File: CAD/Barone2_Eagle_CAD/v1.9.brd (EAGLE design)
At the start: 101.6 x 101.6 mm, 71 parts, among them J2 XT60-M, M1 PIC32MX340F512H-80I/MR, U1 FT232RQ, X1 CB3LV-3C-8M0000, Y1 ABRACON_ASEK-32_768KHZ-LRTABR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

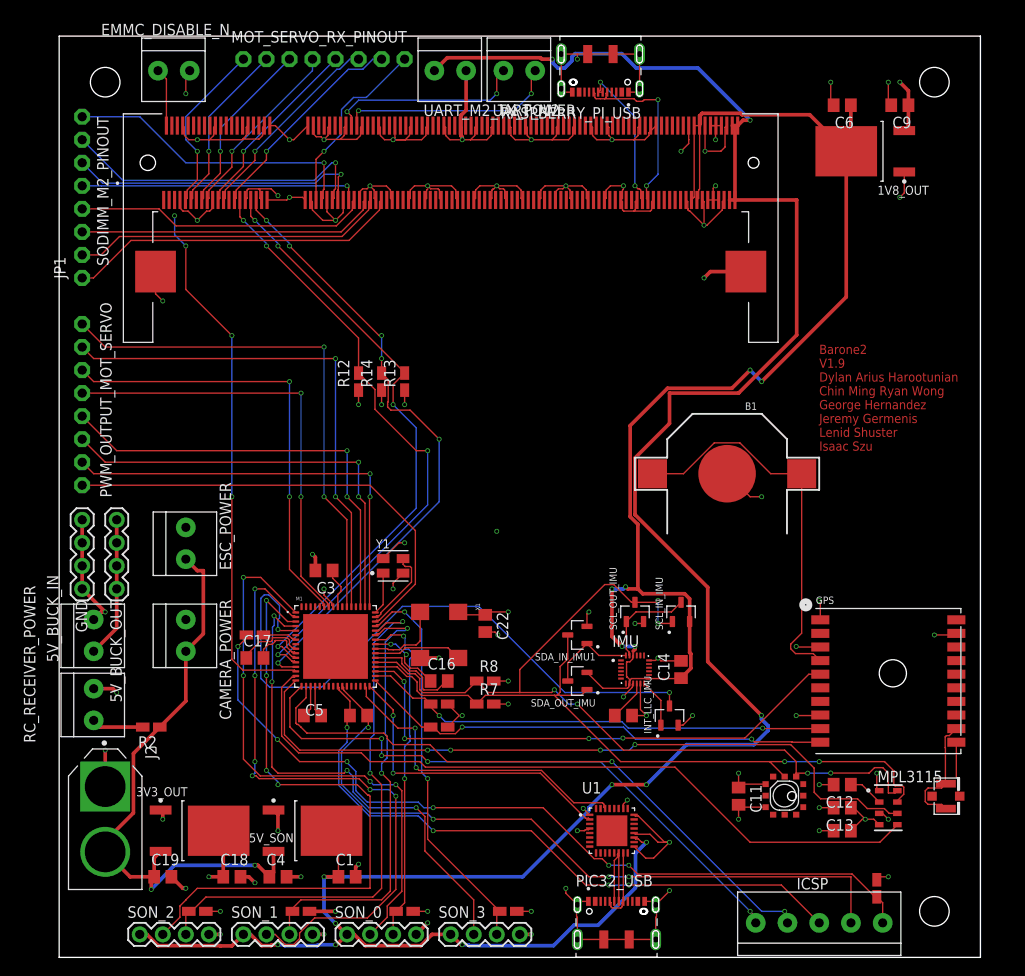
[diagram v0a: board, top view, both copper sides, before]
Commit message: v1.9 finalized and sent to board house OSH Park
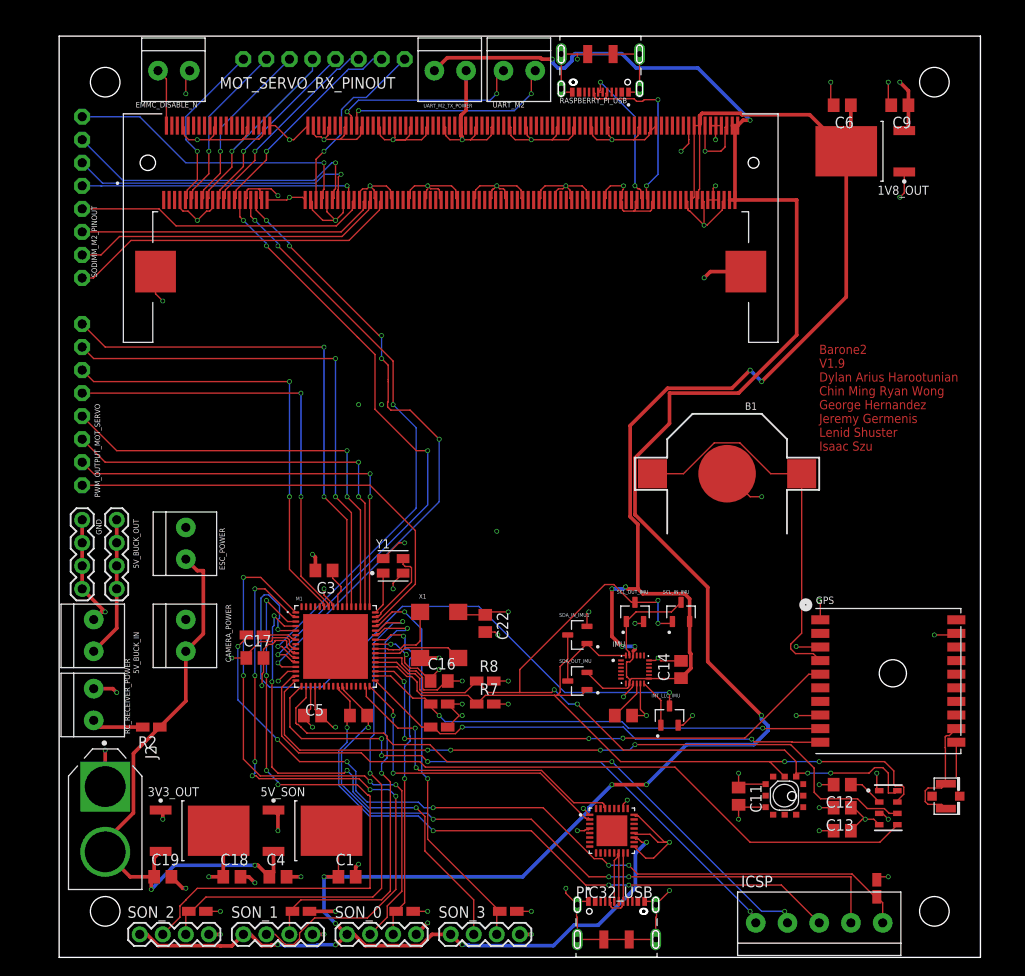
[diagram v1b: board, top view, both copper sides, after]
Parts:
- removed R12, R13, R14: 47k, adafruit:R0805W
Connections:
- removed net AVDD3_M1: C16.2, M1.38
- removed net AVDD_M1: C5.2, M1.19
- removed net AVSS_M1: C5.1, M1.20
- removed net CS_M1: M1.14
- removed net VDD1_M1: C17.2, M1.10
- removed net VDD2_M1: C15.2, ICSP.2, M1.26
- removed net VSS1_M1: C17.1, M1.9
- removed net VSS2_M1: C15.1, ICSP.3, M1.25
- removed net VSS3_M1: C16.1, M1.41
- net GND: now also C15.1, C16.1, C17.1, C5.1, ICSP.3, M1.14, M1.20, M1.25, M1.41, M1.9
- net MISO_M2: no longer R12.2
- net MOSI_M2: no longer R13.2
- net SCK_M2: no longer R14.2
- net VIN: now also C15.2, C16.2, C17.2, C5.2, ICSP.2, M1.10, M1.19, M1.26, M1.38; no longer R12.1, R13.1, R14.1
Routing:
- net GND: track 919.8 -> 1046.8 mm, vias 62 -> 72
- net VIN: track 405.4 -> 524.1 mm, vias 25 -> 32
- net VDD2_M1: track 78.9 -> 0.00 mm, vias 4 -> 0
- net VSS2_M1: track 71.3 -> 0.00 mm, vias 4 -> 0
- net CS_M1: track 59.1 -> 0.00 mm, vias 4 -> 0
- net AVDD3_M1: track 11.0 -> 0.00 mm
- net VSS3_M1: track 8.55 -> 0.00 mm, vias 2 -> 0
- net VSS1_M1: track 7.57 -> 0.00 mm
- net VDD1_M1: track 5.93 -> 0.00 mm
- net AVDD_M1: track 3.54 -> 0.00 mm
- net AVSS_M1: track 3.51 -> 0.00 mm
- net MOSI_M2: track 66.6 -> 65.6 mm
